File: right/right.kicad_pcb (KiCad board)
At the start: 2 copper layers, 92 parts, among them J1 USB_C_Receptacle_USB2.0_16P, J2 AudioJack4, J3 Conn_ARM_JTAG_SWD_10, SW1 SW_RESET, SW10 tab, SW11 q, SW12 w, SW13 e, SW14 r, SW15 t, SW16 [, SW17 caps, SW18 a, SW19 s, SW2 SW_BOOT, SW20 d, SW21 f, SW22 g, SW23 ->, SW24 shift, SW25 z, SW26 x, SW27 c, SW28 v, SW29 b, SW3 `, SW30 custom2, SW31 ctrl, SW32 menu, SW33 alt, SW34 space, SW35 space, SW4 1, SW5 2, SW6 3, SW7 4, SW8 5, SW9 -, U1 LM3480-3.3, U2 STM32F072CBTx, Y1 8MHz

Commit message: Finish right halve
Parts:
- J3: moved to B.Cu
- SW24: value shift -> z
- moved SW31 143.3 mm to (79.2, 103.6), turned to 30 degrees
- moved J3 51.4 mm to (18.5, 74.4), turned to 180 degrees
- moved SW25 48.2 mm to (83.2, 81.6), turned to 0 degrees
- moved SW10 43.6 mm to (64.2, 55.4)
- moved SW11 43.6 mm to (83.2, 43.5)
- moved SW13 43.6 mm to (121.3, 38.8)
- moved SW14 43.6 mm to (140.4, 41.2)
- moved SW15 43.6 mm to (159.6, 43.5)
- moved SW16 43.6 mm to (178.5, 43.5)
- moved SW17 43.6 mm to (64.2, 74.5)
- moved SW18 43.6 mm to (83.2, 62.6)
- moved SW20 43.6 mm to (121.3, 57.8)
- moved SW21 43.6 mm to (140.4, 60.2)
- moved SW22 43.6 mm to (159.4, 62.6)
- moved SW23 43.6 mm to (178.5, 62.6)
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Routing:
- net Col4: track 0.00 -> 226.0 mm, vias 0 -> 1
- net Col6: track 0.00 -> 225.7 mm, vias 0 -> 1
- net Col3: track 0.00 -> 204.0 mm, vias 0 -> 1
- net Col5: track 0.00 -> 203.3 mm, vias 0 -> 1
- net Net-(D7-A): track 0.00 -> 197.6 mm
- net Col2: track 0.00 -> 181.7 mm, vias 0 -> 1
- net Net-(D6-A): track 0.00 -> 181.2 mm
- net Net-(D33-A): track 0.00 -> 172.9 mm
- net Net-(D14-A): track 0.00 -> 170.8 mm
- net Net-(D5-A): track 0.00 -> 163.4 mm
- net Net-(D21-A): track 0.00 -> 161.2 mm
- net Col1: track 0.00 -> 157.9 mm, vias 0 -> 1
- net Net-(D28-A): track 0.00 -> 156.3 mm
- net Net-(D32-A): track 0.00 -> 156.2 mm
- net Net-(D13-A): track 0.00 -> 154.5 mm
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- added copper zone on B.Cu, net GND
- added copper zone on F.Cu, net GND
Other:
- board outline added: 175.1 x 120 mm

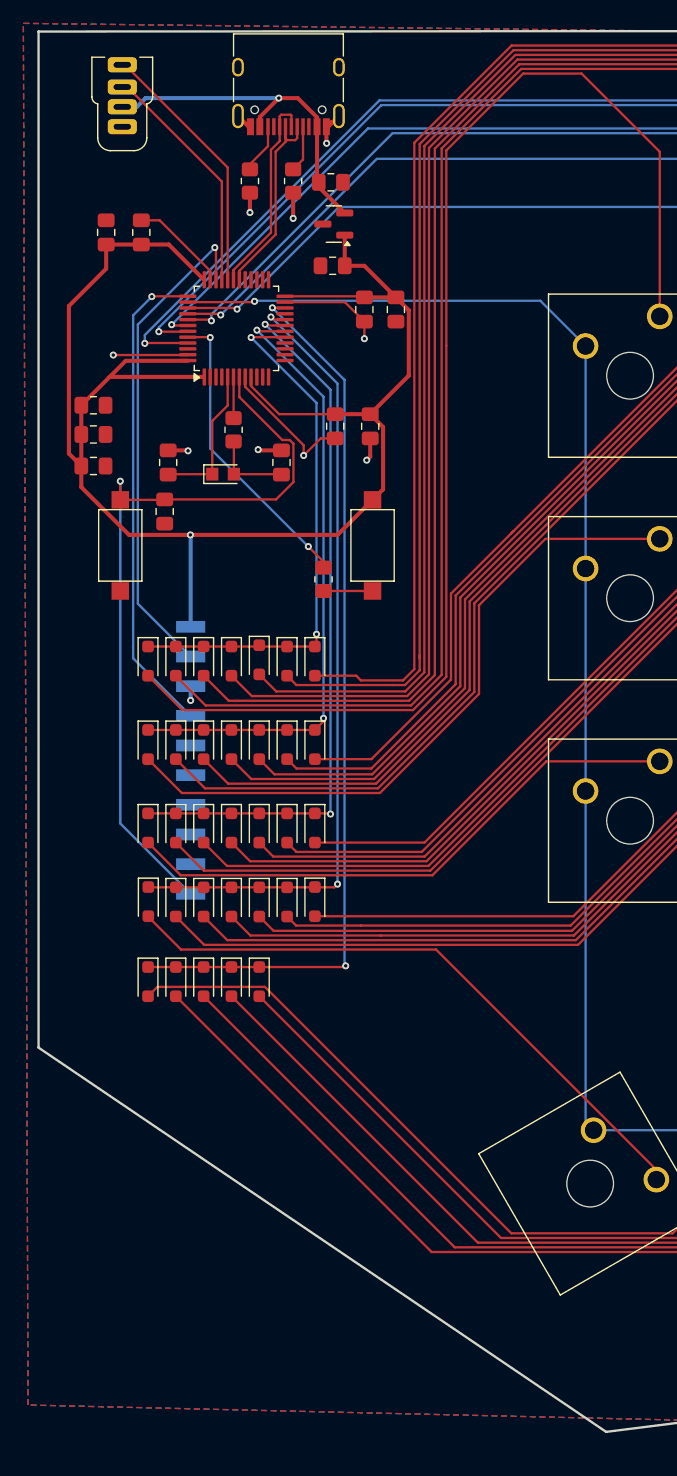
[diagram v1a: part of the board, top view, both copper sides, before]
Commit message: left halve plate holes & python script
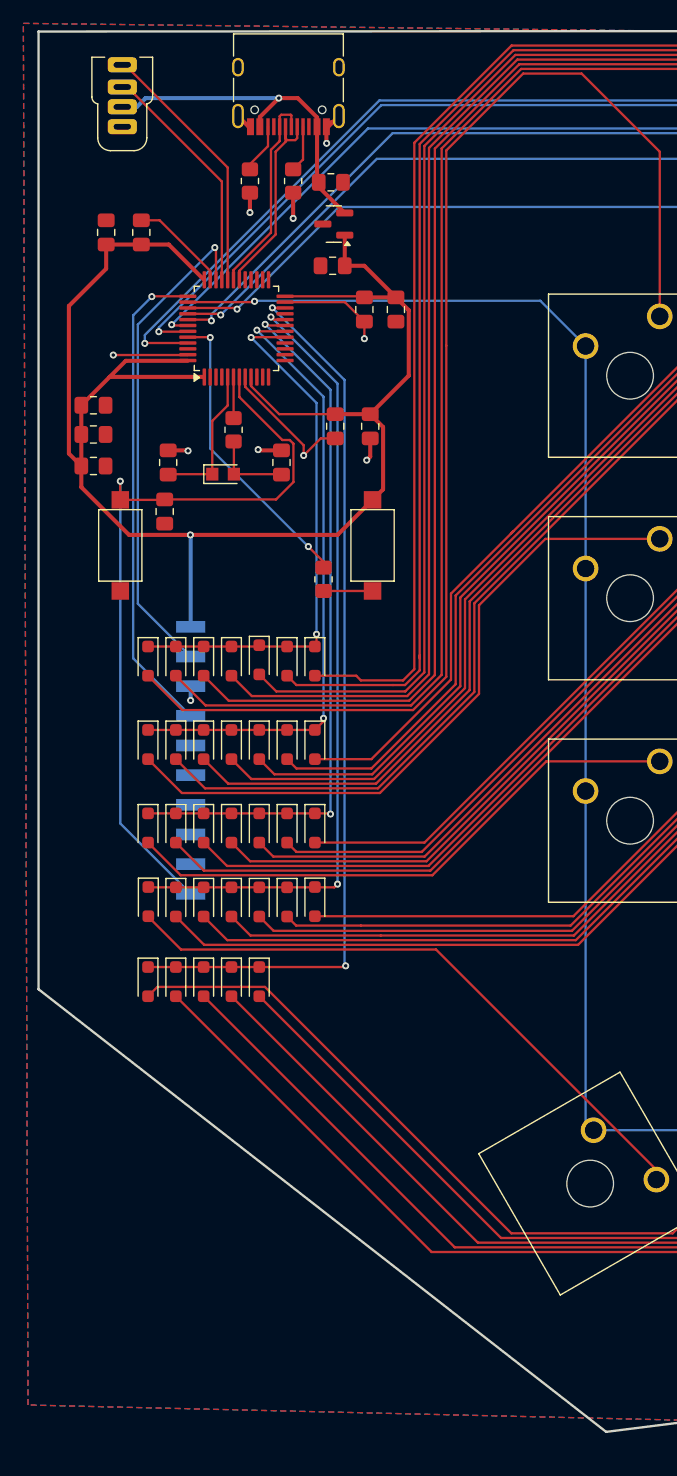
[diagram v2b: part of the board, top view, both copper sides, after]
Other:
- outline, holes or cut-outs redrawn
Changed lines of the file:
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@@
 	)
 	(gr_line
-		(start 11 99)
+		(start 11 94)
 		(end 59.6 131.9)
 		(stroke
@@
 	(gr_line
 		(start 11 12)
-		(end 11 99)
+		(end 11 94)
 		(stroke
 			(width 0.2)

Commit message: change cristals
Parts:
- removed R4: 390, Resistor_SMD:R_0805_2012Metric_Pad1.20x1.40mm_HandSolder
- Y1: footprint Crystal:Crystal_SMD_2012-2Pin_2.0x1.2mm_HandSoldering -> Crystal:Crystal_SMD_3225-4Pin_3.2x2.5mm_HandSoldering
- moved Y1 2.38 mm to (27.1, 47.5)
- moved J2 1.57 mm to (17.9, 13.3)
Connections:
- C14 pad 1: Net-(C14-Pad1) -> Net-(U2-PF1)
- Y1 pad 2: Net-(C14-Pad1) -> GND
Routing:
- net Net-(C14-Pad1): track 6.90 -> 0.00 mm
- net Net-(U2-PF1): track 3.52 -> 10.2 mm
- net GND: track 52.2 -> 57.6 mm, vias 10 -> 11
- net RX: track 22.3 -> 24.5 mm
- net TX: track 20.3 -> 22.4 mm
- net Net-(U2-PF0): track 12.7 -> 11.8 mm
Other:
- board text added: "Designed in Chicago"
- board text added: "Tastiera v0.1"
